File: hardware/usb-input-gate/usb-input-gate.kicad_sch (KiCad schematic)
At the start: 10 parts, among them J201 RAW USB POWER, J202 TO INPUT INTEGRATION, J203 SOURCE LOGIC, U201 TPS25200DRVR

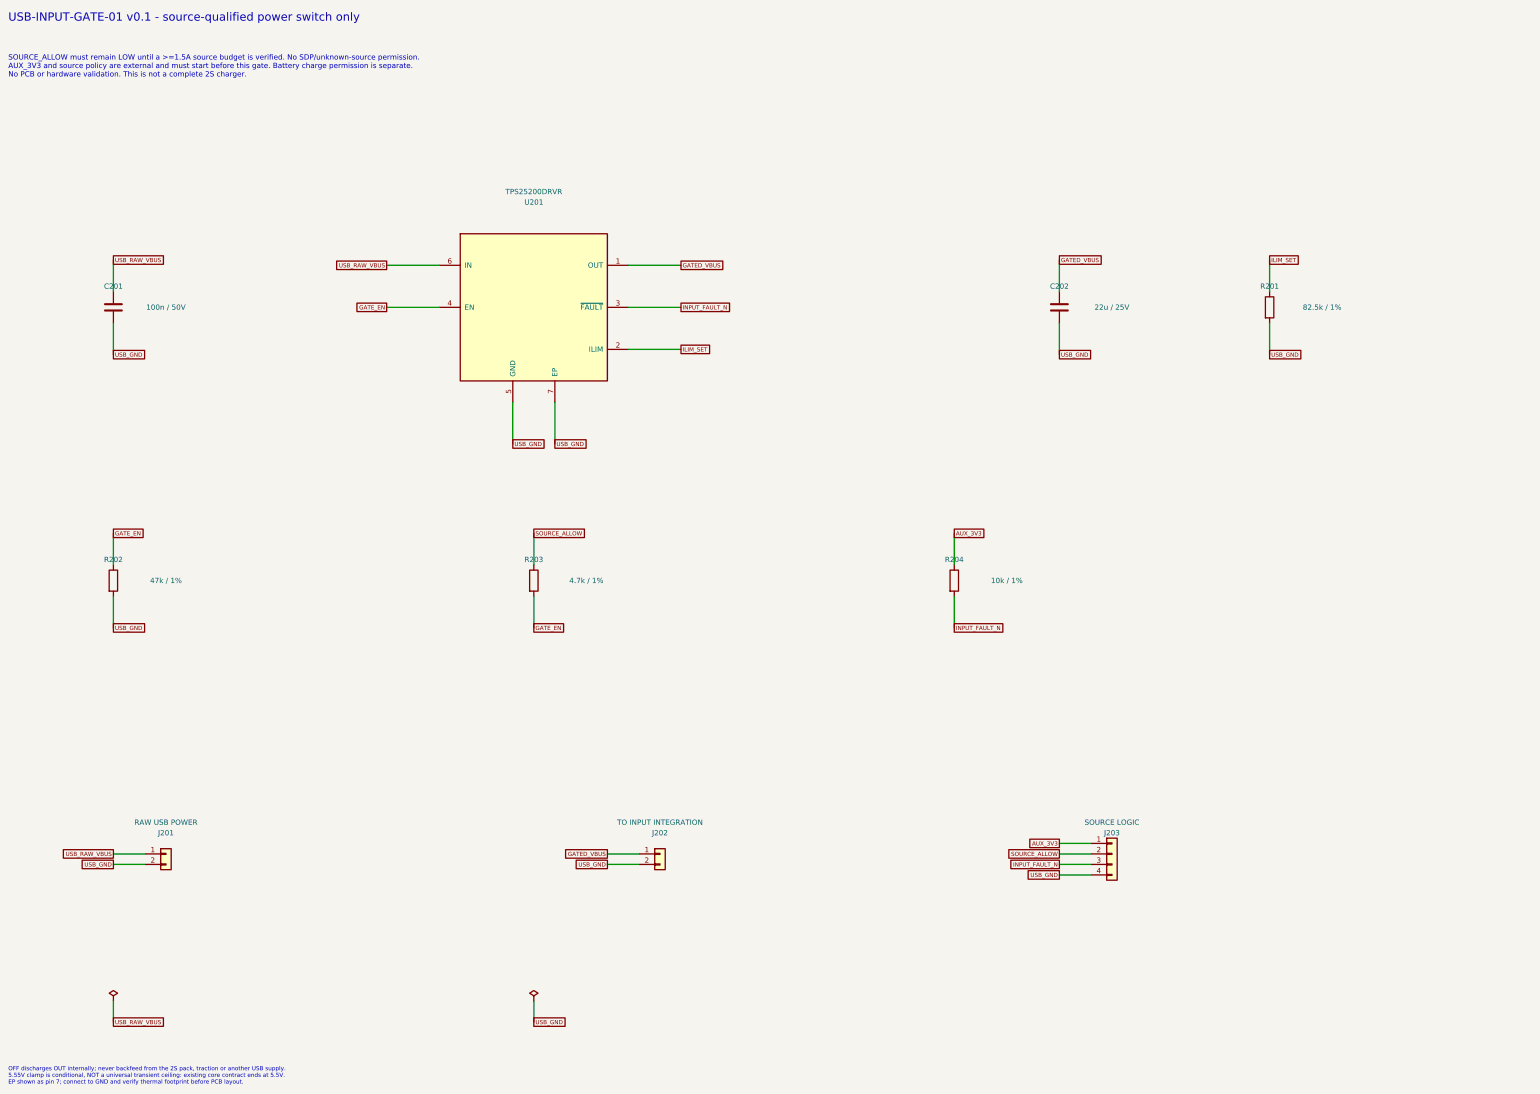
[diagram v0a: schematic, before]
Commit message: hardware: add independent USB auxiliary supply for source detection
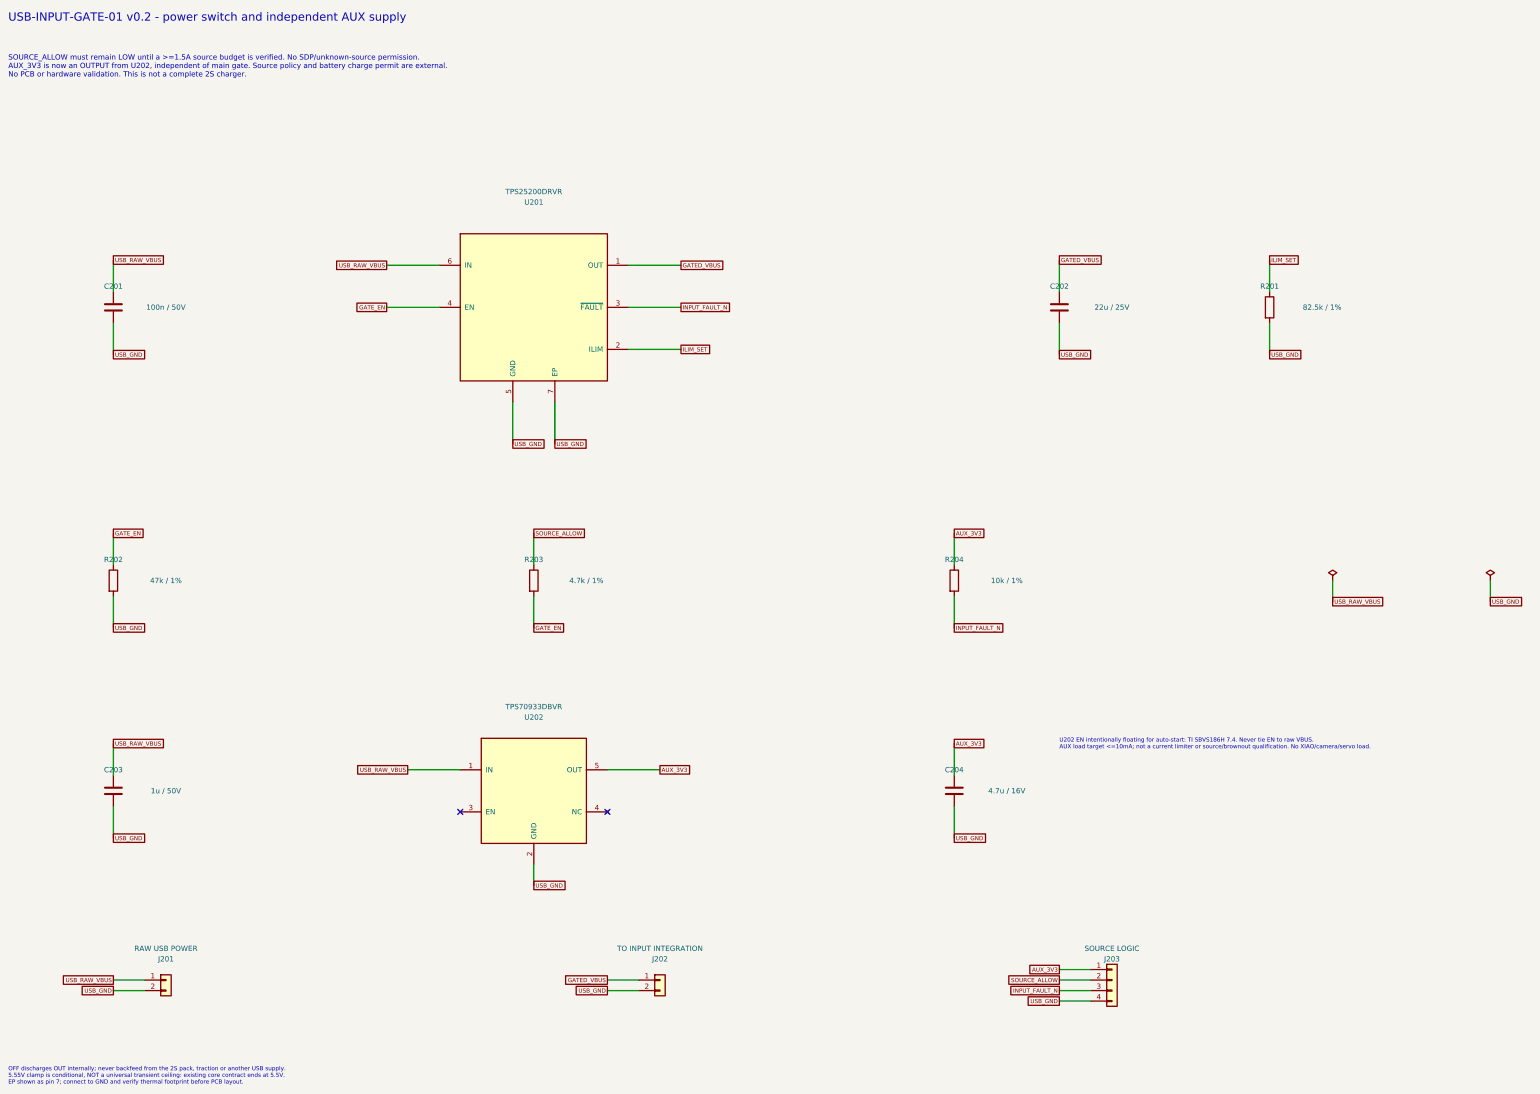
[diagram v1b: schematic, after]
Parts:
- added C203: 1u / 50V, symbol RaceRemote_Input:C
- added C204: 4.7u / 16V, symbol RaceRemote_Input:C
- added U202: TPS70933DBVR, symbol RaceRemote_Input:TPS70933DBV
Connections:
- net AUX_3V3: now also C204.1, U202.5 (OUT)
- net USB_GND: now also C203.2, C204.2, U202.2 (GND)
- net USB_RAW_VBUS: now also C203.1, U202.1 (IN)
- no-connect marks 0 -> 2
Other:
- note added: "SOURCE_ALLOW must remain LOW until a >=1.5A source budget is verified. No SDP/unknown-source permission. AUX_3V3 is now an OUTPUT from U202, independent of main gate. Source policy and battery charge permit are external. No PCB or hardware validation. This is not a complete 2S charger."
- note added: "U202 EN intentionally floating for auto-start: TI SBVS186H 7.4. Never tie EN to raw VBUS. AUX load target <=10mA; not a current limiter or source/brownout qualification. No XIAO/camera/servo load."
- note added: "USB-INPUT-GATE-01 v0.2 - power switch and independent AUX supply"
- note removed: "SOURCE_ALLOW must remain LOW until a >=1.5A source budget is verified. No SDP/unknown-source permission. AUX_3V3 and source policy are external and must start before this gate. Battery charge permission is separate. No PCB or hardware validation. This is not a complete 2S charger."
- note removed: "USB-INPUT-GATE-01 v0.1 - source-qualified power switch only"
- moved on the sheet: J201, J202, J203
